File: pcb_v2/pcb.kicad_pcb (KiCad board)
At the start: 2 copper layers, 229.9 x 97.8 mm, 153 parts, among them J1 USB_C_Receptacle_USB2.0, SW1 Reset, SW10 SW_Push, SW11 SW_Push, SW12 SW_Push, SW13 SW_Push, SW14 SW_Push, SW15 SW_Push, SW16 SW_Push, SW17 SW_Push, SW18 SW_Push, SW19 SW_Push, SW2 SW_Push, SW20 SW_Push, SW21 SW_Push, SW22 SW_Push, SW23 SW_Push, SW24 SW_Push, SW25 SW_Push, SW26 SW_Push, SW27 SW_Push, SW28 SW_Push, SW29 SW_Push, SW3 SW_Push, SW30 SW_Push, SW31 SW_Push, SW32 SW_Push, SW33 SW_Push, SW34 SW_Push, SW35 SW_Push, SW36 SW_Push, SW37 SW_Push, SW38 SW_Push, SW39 SW_Push, SW4 SW_Push, SW40 SW_Push, SW41 SW_Push, SW42 SW_Push, SW43 SW_Push, SW44 SW_Push, SW45 SW_Push, SW46 SW_Push, SW47 SW_Push, SW48 SW_Push, SW49 SW_Push, SW5 SW_Push, SW50 SW_Push, SW51 SW_Push, SW52 SW_Push, SW53 SW_Push, SW54 SW_Push, SW55 SW_Push, SW56 SW_Push, SW57 SW_Push, SW58 SW_Push, SW59 SW_Push, SW6 SW_Push, SW60 SW_Push, SW7 SW_Push, SW8 SW_Push, SW9 SW_Push, U1 ATmega32U4-AU, Y1 TSX3225

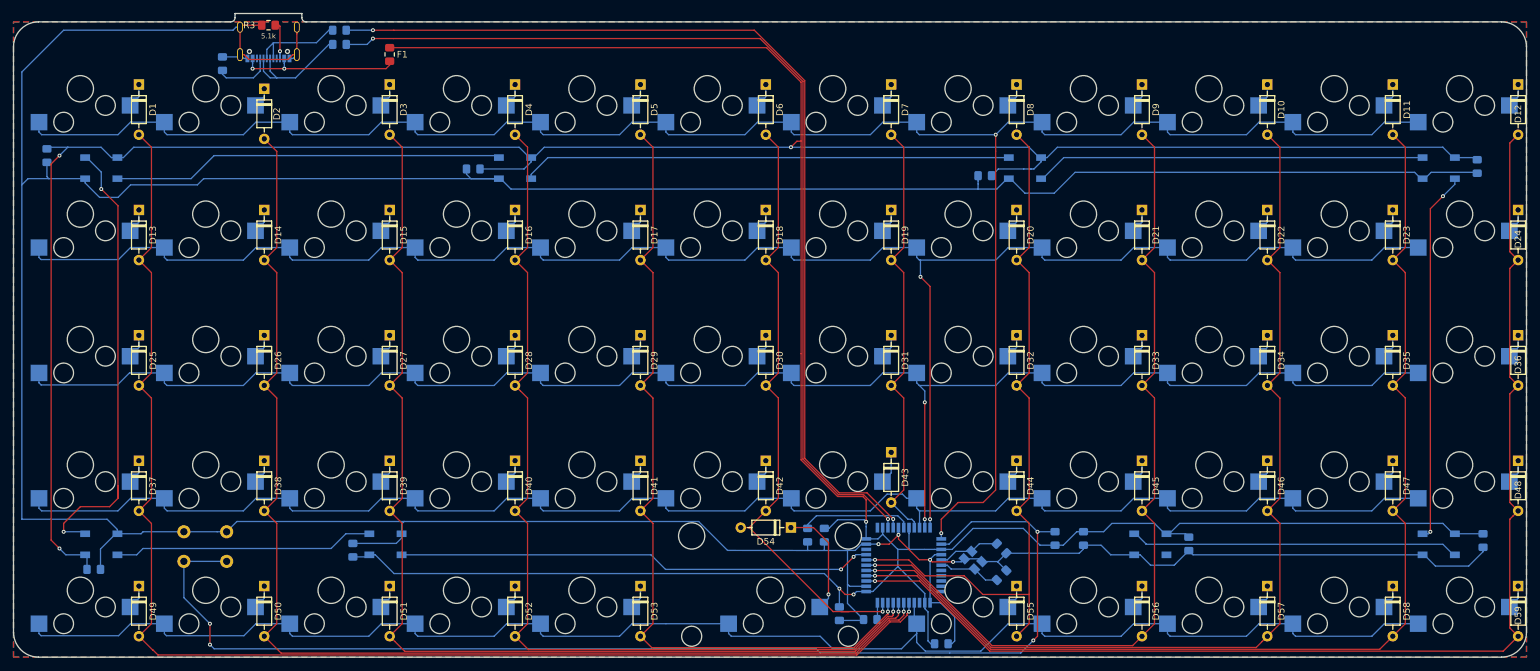
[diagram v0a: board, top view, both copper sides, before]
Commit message: Upgrade to latest KiCAD and tweak measurements
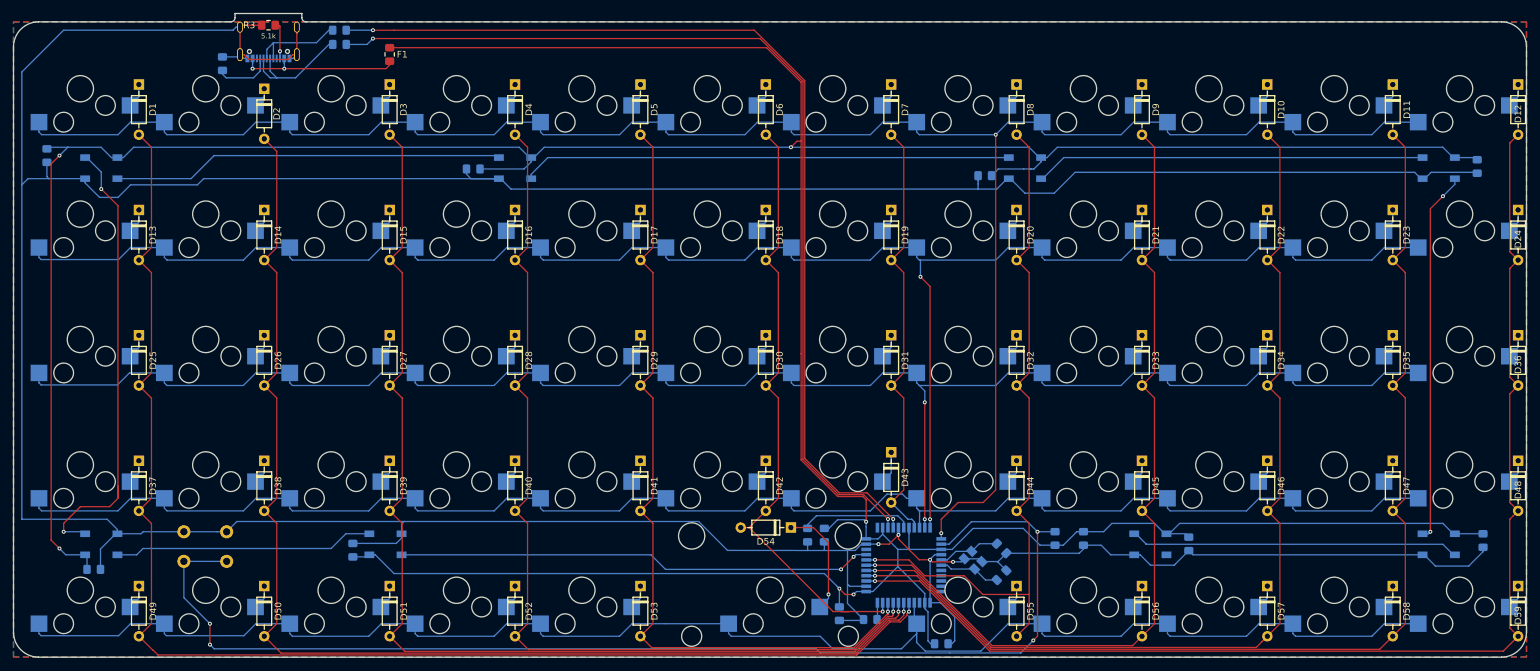
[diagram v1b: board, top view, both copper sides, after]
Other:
- net class Default removed
